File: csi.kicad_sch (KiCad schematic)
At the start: 99 parts, among them J7 WE_68715014522, J8 WE_68715014522, Q5 NX138BKMYL, Q6 NX138BKMYL, Q7 NX138BKMYL, Q8 NX138BKMYL, U24 AP22653FDZ-7, U25 AP22653FDZ-7, U26 PCA9547BS, U27 AP22653FDZ-7, U28 AP22653FDZ-7, U31 NTS0102GT, U32 NTS0102GT

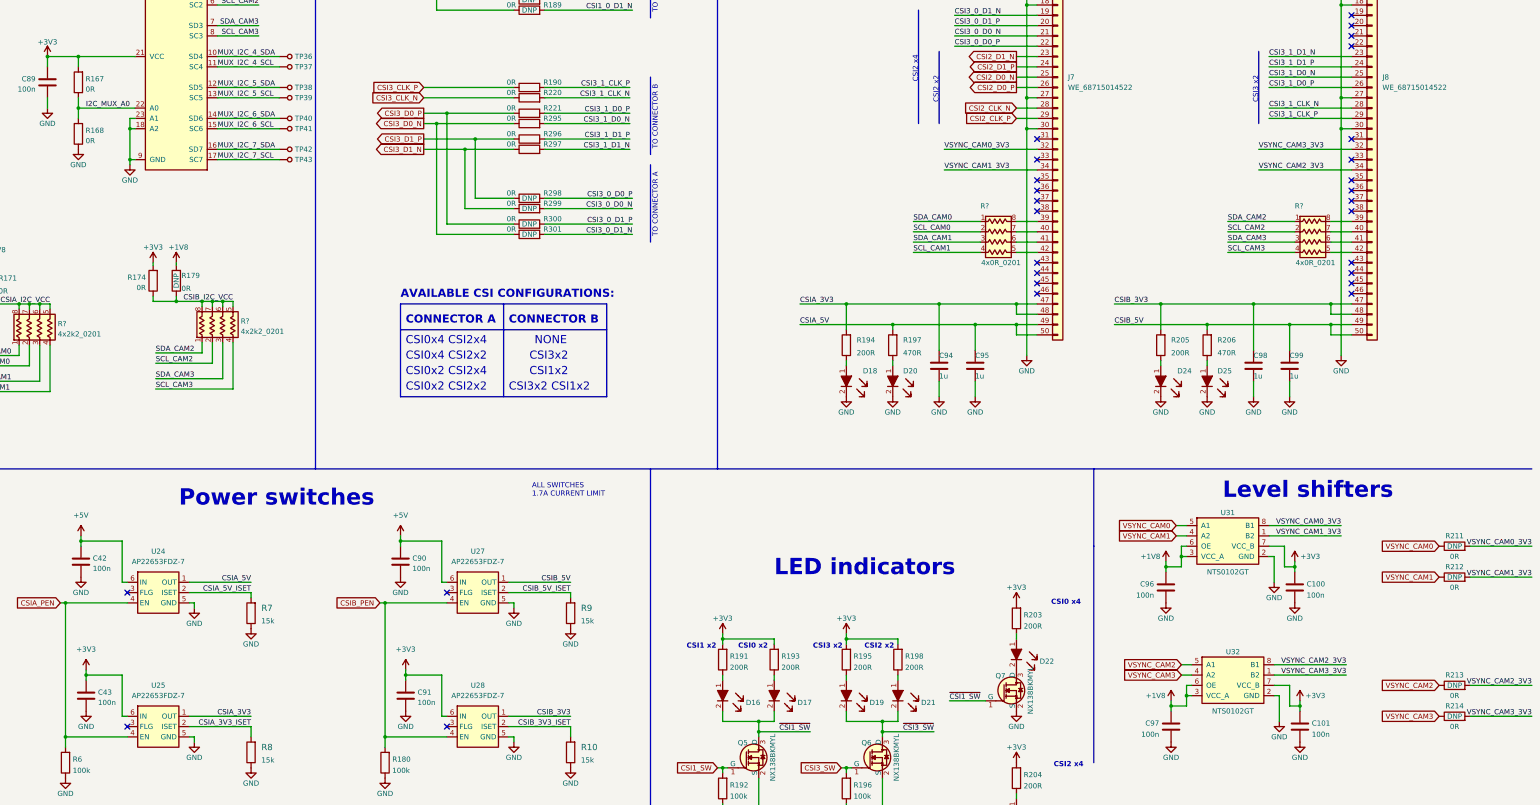
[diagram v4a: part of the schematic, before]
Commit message: Replace part of 0R resistors with resistor arrays
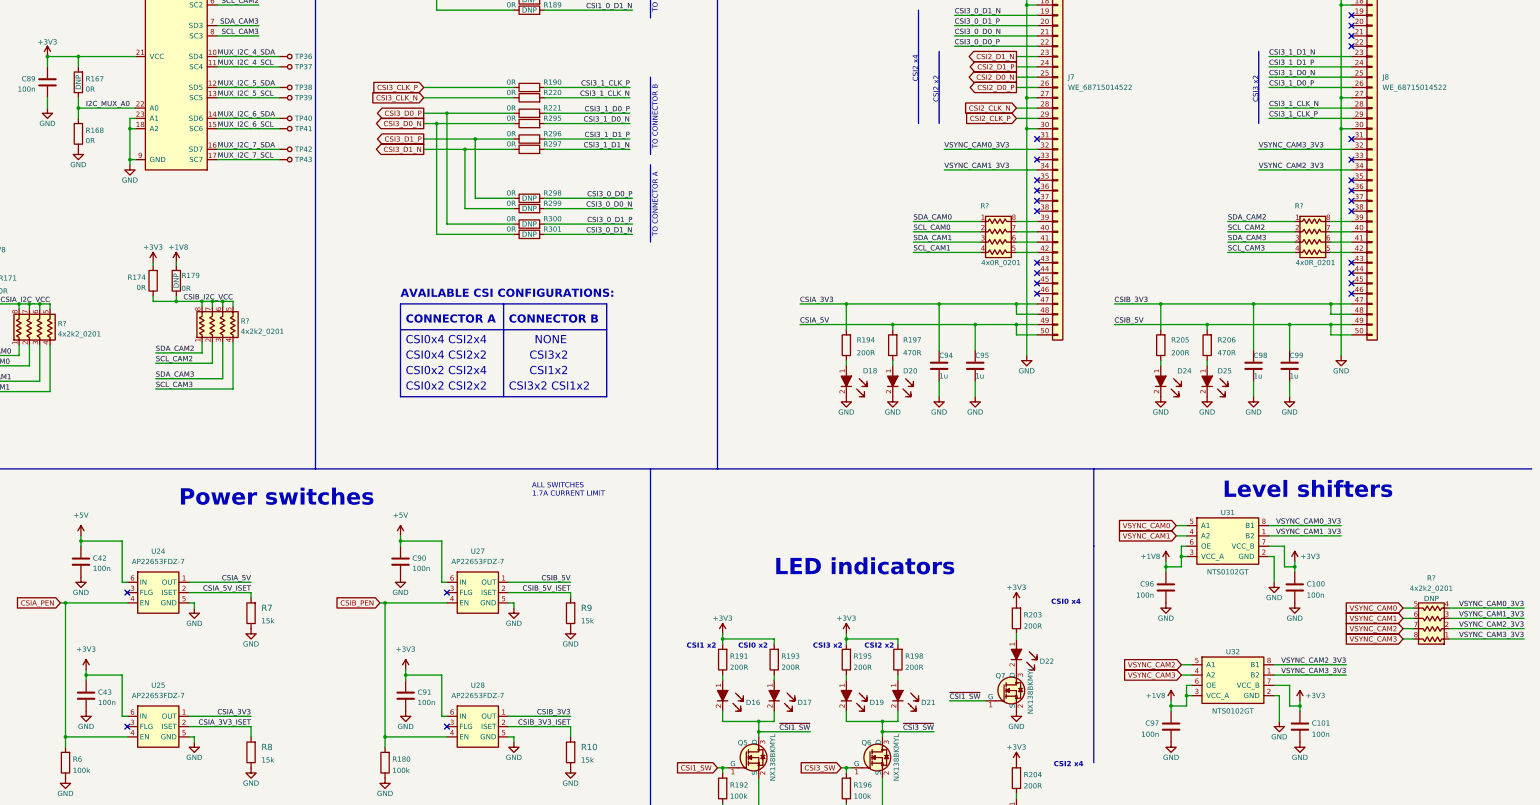
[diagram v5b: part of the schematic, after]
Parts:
- removed R211, R212, R213, R214: R_0R_0402, antmicro-footprints:0402-res, symbol antmicroResistors0402:R_0R_0402
- added R?: 4x2k2_0201_array, antmicro-footprints:EXB18V, symbol antmicroResistorNetworksArrays:4x2k2_0201_array
- R167: DNP (none) -> DNP
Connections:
- net VSYNC_CAM0: now also R?.5
- net VSYNC_CAM0_3V3: now also R?.4
- net VSYNC_CAM1: now also R?.6
- net VSYNC_CAM1_3V3: now also R?.3
- net VSYNC_CAM2: now also R?.7
- net VSYNC_CAM2_3V3: now also R?.2
- net VSYNC_CAM3: now also R?.8
- net VSYNC_CAM3_3V3: now also R?.1

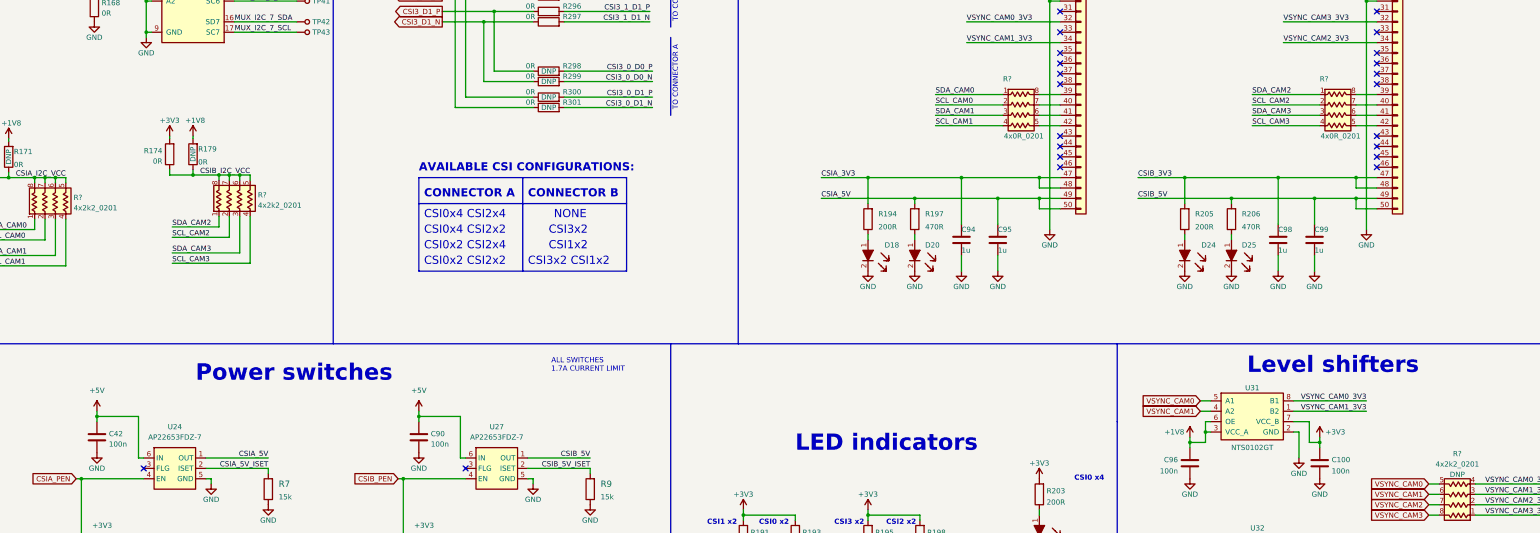
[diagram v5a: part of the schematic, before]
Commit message: Minor cleanup, annotate parts, import them to PCB
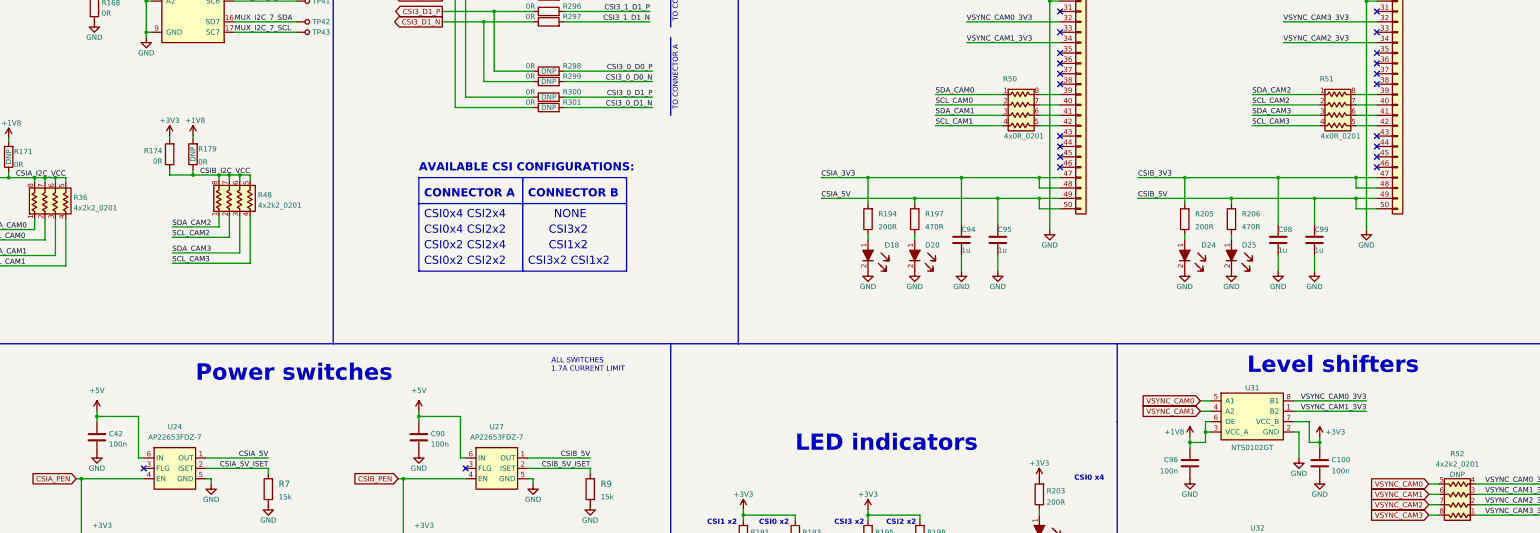
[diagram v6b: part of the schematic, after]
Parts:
- gave numbers to parts that had none: 5
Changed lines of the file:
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@@
   (symbol (lib_id "antmicroResistorNetworksArrays:4x2k2_0201_array") (at 382.27 212.09 180) (unit 1)
     (in_bom yes) (on_board yes) (fields_autoplaced)
-    (property "Reference" "R?" (id 0) (at 382.905 207.2504 0))
+    (property "Reference" "R52" (id 0) (at 382.905 207.2504 0))
     (property "Value" "4x2k2_0201_array" (id 1) (at 382.27 209.55 0)
       (effects (font (size 1.524 1.524)) hide)
@@
   (symbol (lib_id "power:+3V3") (at 67.945 129.54 0) (unit 1)
     (in_bom yes) (on_board yes)
-    (property "Reference" "#PWR?" (id 0) (at 67.945 133.35 0)
+    (property "Reference" "#PWR0163" (id 0) (at 67.945 133.35 0)
       (effects (font (size 1.27 1.27)) hide)
     )
@@
   (symbol (lib_id "power:+1V8") (at 73.66 129.54 0) (unit 1)
     (in_bom yes) (on_board yes)
-    (property "Reference" "#PWR?" (id 0) (at 73.66 133.35 0)
+    (property "Reference" "#PWR0166" (id 0) (at 73.66 133.35 0)
       (effects (font (size 1.27 1.27)) hide)
     )
@@
   (symbol (lib_id "antmicroResistorNetworksArrays:4x2k2_0201_array") (at 45.085 144.78 90) (unit 1)
     (in_bom yes) (on_board yes) (fields_autoplaced)
-    (property "Reference" "R?" (id 0) (at 44.45 144.5803 90)
+    (property "Reference" "R36" (id 0) (at 44.45 144.5803 90)
       (effects (font (size 1.27 1.27)) (justify right))
     )
@@
   (symbol (lib_name "4x0R_0201_array_1") (lib_id "antmicroResistorNetworksArrays:4x0R_0201_array") (at 276.86 129.54 0) (unit 1)
     (in_bom yes) (on_board yes) (fields_autoplaced)
-    (property "Reference" "R?" (id 0) (at 271.78 115.57 0)
+    (property "Reference" "R50" (id 0) (at 271.78 115.57 0)
       (effects (font (size 1.27 1.27)) (justify left))
     )
@@
   (symbol (lib_id "antmicroResistorNetworksArrays:4x2k2_0201_array") (at 90.17 144.145 90) (unit 1)
     (in_bom yes) (on_board yes) (fields_autoplaced)
-    (property "Reference" "R?" (id 0) (at 89.535 143.9453 90)
+    (property "Reference" "R48" (id 0) (at 89.535 143.9453 90)
       (effects (font (size 1.27 1.27)) (justify right))
     )
@@
   (symbol (lib_name "4x0R_0201_array_2") (lib_id "antmicroResistorNetworksArrays:4x0R_0201_array") (at 354.33 129.54 0) (unit 1)
     (in_bom yes) (on_board yes) (fields_autoplaced)
-    (property "Reference" "R?" (id 0) (at 349.25 115.57 0)
-      (effects (font (size 1.27 1.27)) (justify left))
-    )
+    (property "Reference" "R51" (id 0) (at 349.25 115.57 0)
+      (effects (font (size 1.27 1.27)) (justify left))
+    )

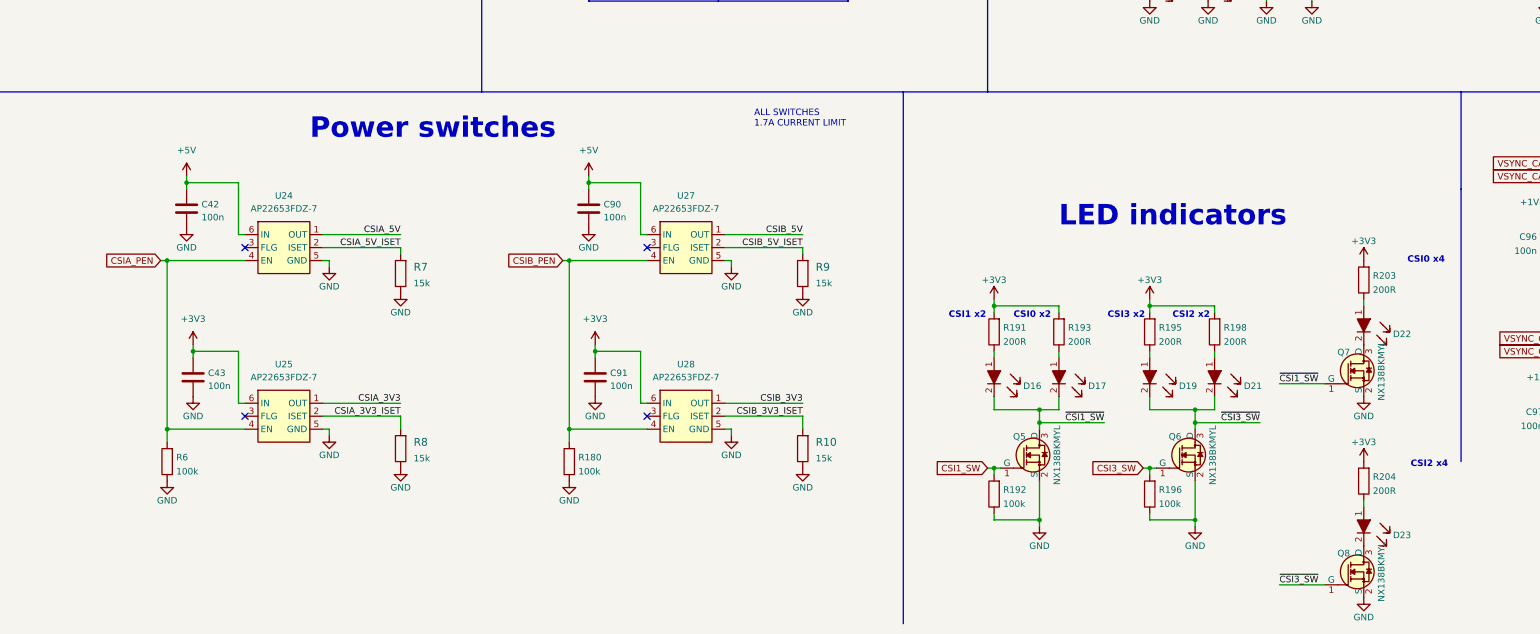
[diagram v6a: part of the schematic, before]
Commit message: Removed CSI mux LEDs and unified component types
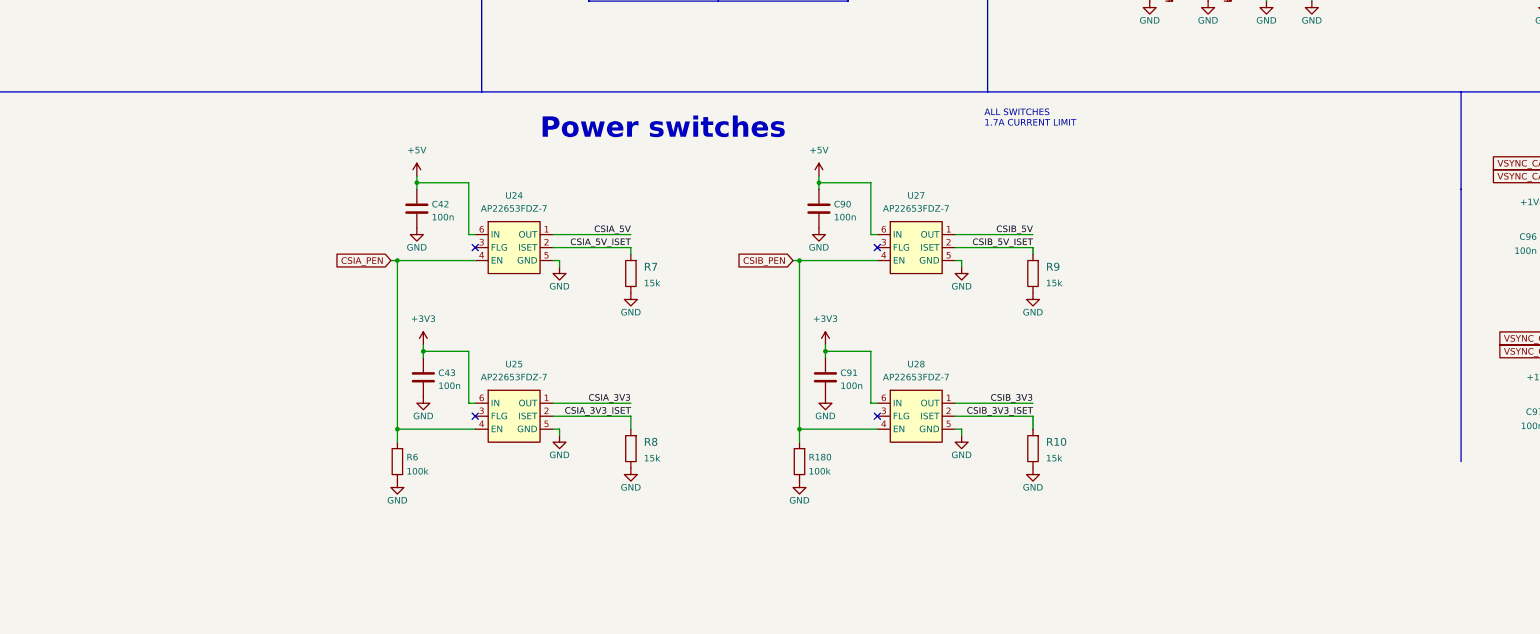
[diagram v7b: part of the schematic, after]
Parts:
- removed D16, D17, D19, D21, D22, D23: LTST-C190GKT, antmicro-footprints:LED_0603, symbol antmicroLEDIndicationDiscrete:LTST-C190GKT
- removed Q5, Q6, Q7, Q8: NX138BKMYL, antmicro-footprints:DFN1006-3, symbol antmicroTransistorsFETsMOSFETsSingle:NX138BKMYL
- removed R191, R193, R195, R198, R203, R204: R_200R_0402, antmicro-footprints:0402-res, symbol antmicroResistors0402:R_200R_0402
- removed R192, R196: R_100k_0402, antmicro-footprints:0402-res, symbol antmicroResistors0402:R_100k_0402
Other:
- note removed: "LED indicators"
- moved on the sheet: C42, C43, C90, C91, R10, R180, R6, R7, R8, R9, U24, U25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

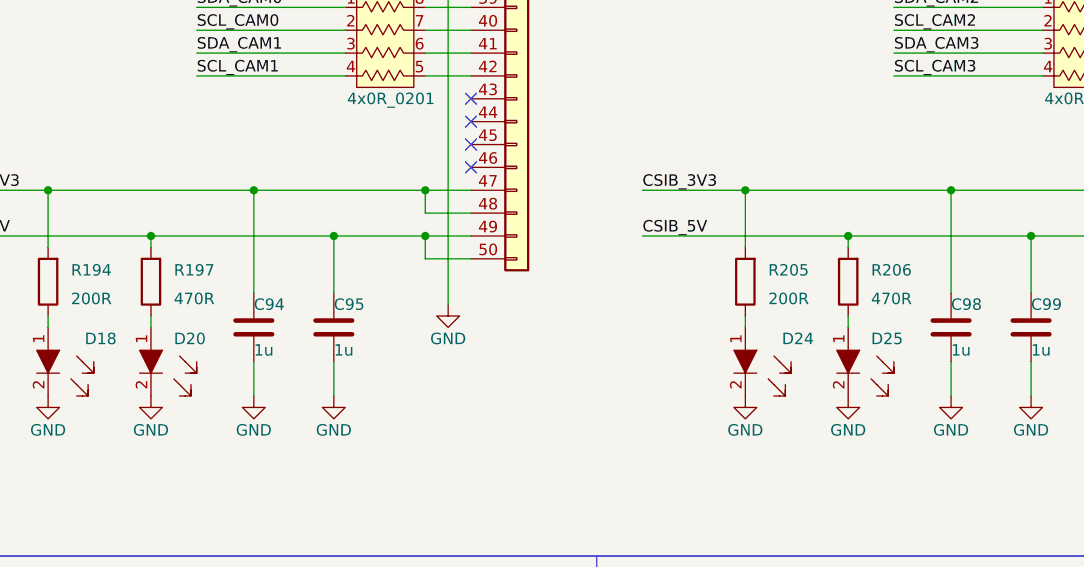
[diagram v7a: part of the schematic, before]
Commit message: Rearanged PCB to move M.2 connector and changed exp conn resistors to res arrays
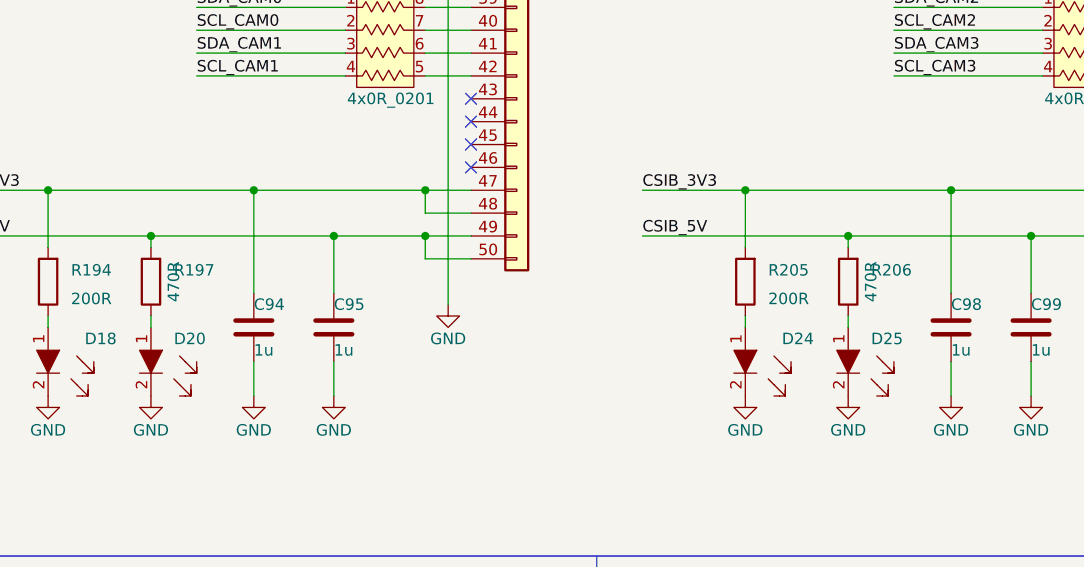
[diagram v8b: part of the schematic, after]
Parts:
- R197, R206: value R_470R_0603 -> R_470R_0402; footprint antmicro-footprints:0603-res -> antmicro-footprints:0402-res; symbol antmicroResistors0603:R_470R_0603 -> antmicroResistors0402:R_470R_0402; MPN CR0603-JW-471GLF -> CRCW0402470RFKED; Manufacturer BOURNS -> VISHAY
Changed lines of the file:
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@@
     (pin "2")
   )
-  (symbol (lib_id "antmicroResistors0603:R_470R_0603") (at 327.66 149.86 90) (unit 1)
+  (symbol (lib_id "antmicroResistors0402:R_470R_0402") (at 327.66 149.86 90) (unit 1)
     (in_bom yes) (on_board yes) (fields_autoplaced)
     (property "Reference" "R206" (id 0) (at 330.2 148.59 90)
       (effects (font (size 1.27 1.27)) (justify right))
     )
-    (property "Value" "R_470R_0603" (id 1) (at 331.47 149.86 0)
-      (effects (font (size 1.27 1.27)) hide)
+    (property "Value" "R_470R_0402" (id 1) (at 331.47 149.86 0)
+      (effects (font (size 1.524 1.524)) hide)
     )
-    (property "Footprint" "antmicro-footprints:0603-res" (id 2) (at 322.58 144.78 0)
+    (property "Footprint" "antmicro-footprints:0402-res" (id 2) (at 322.58 144.78 0)
       (effects (font (size 1.524 1.524)) (justify left) hide)
     )
@@
       (effects (font (size 1.27 1.27)) hide)
     )
-    (property "Manufacturer" "BOURNS" (id 4) (at 317.5 144.78 0)
+    (property "Manufacturer" "VISHAY" (id 4) (at 317.5 144.78 0)
       (effects (font (size 1.524 1.524)) (justify left) hide)
     )
-    (property "MPN" "CR0603-JW-471GLF" (id 5) (at 320.04 144.78 0)
+    (property "MPN" "CRCW0402470RFKED" (id 5) (at 320.04 144.78 0)
       (effects (font (size 1.524 1.524)) (justify left) hide)
     )
-    (property "Val" "470R" (id 6) (at 330.2 151.7649 90)
-      (effects (font (size 1.27 1.27)) (justify right))
-    )
+    (property "Val" "470R" (id 6) (at 330.2 149.86 0))
     (pin "1")
     (pin "2")
@@
     (pin "2")
   )
-  (symbol (lib_id "antmicroResistors0603:R_470R_0603") (at 250.19 149.86 90) (unit 1)
+  (symbol (lib_id "antmicroResistors0402:R_470R_0402") (at 250.19 149.86 90) (unit 1)
     (in_bom yes) (on_board yes) (fields_autoplaced)
     (property "Reference" "R197" (id 0) (at 252.73 148.59 90)
       (effects (font (size 1.27 1.27)) (justify right))
     )
-    (property "Value" "R_470R_0603" (id 1) (at 254 149.86 0)
-      (effects (font (size 1.27 1.27)) hide)
+    (property "Value" "R_470R_0402" (id 1) (at 254 149.86 0)
+      (effects (font (size 1.524 1.524)) hide)
     )
-    (property "Footprint" "antmicro-footprints:0603-res" (id 2) (at 245.11 144.78 0)
+    (property "Footprint" "antmicro-footprints:0402-res" (id 2) (at 245.11 144.78 0)
       (effects (font (size 1.524 1.524)) (justify left) hide)
     )
@@
       (effects (font (size 1.27 1.27)) hide)
     )
-    (property "Manufacturer" "BOURNS" (id 4) (at 240.03 144.78 0)
+    (property "Manufacturer" "VISHAY" (id 4) (at 240.03 144.78 0)
       (effects (font (size 1.524 1.524)) (justify left) hide)
     )
-    (property "MPN" "CR0603-JW-471GLF" (id 5) (at 242.57 144.78 0)
+    (property "MPN" "CRCW0402470RFKED" (id 5) (at 242.57 144.78 0)
       (effects (font (size 1.524 1.524)) (justify left) hide)
     )
-    (property "Val" "470R" (id 6) (at 252.73 151.7649 90)
-      (effects (font (size 1.27 1.27)) (justify right))
-    )
+    (property "Val" "470R" (id 6) (at 252.73 149.86 0))
     (pin "1")
     (pin "2")
